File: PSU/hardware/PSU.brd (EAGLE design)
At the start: 143.5 x 58.5 mm, 211 parts, among them J1 SWD, J2 UART, Q1 PMOS-DPAK, Q10 PMOS-SOT23, Q11 NPN, Q12 PMOS-SOT23, Q13 NPN, Q14 NPN, Q15 PMOS-SOT23, Q2 PMOS-SOT23, Q3 NPN, Q4 PMOS-SOT23, Q5 NMOS-SOT23, Q6 PMOS-DPAK, Q7 PMOS-SOT23, Q8 NMOS-SOT23, Q9 PMOS-DPAK, U1 LM2576, U10 4069, U11 LTV-247, U12 74HC08, U13 STM8S003K3T6C, U14 74HC08, U15 4051, U16 358, U17 358, U18 74HC32, U2 MT3608, U3 7805, U4 324, U5 MC34063, U6 MT3608, U7 LM2576, U8 MC34063, U9 TP4056

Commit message: [HW/PSU] Add switch debouncing
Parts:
- added C28, C29: 100n, rcl:C0805
- added R82: 100k, rcl:R0805
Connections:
- net GND: now also C28.2, C29.2, R82.1
- net VBACKUP: now also R82.2
- net ^HDDON: now also C29.1
- net ^PWRON: now also C28.1
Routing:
- net VBACKUP: track 178.1 -> 180.3 mm
- net ^HDDON: track 66.6 -> 68.4 mm
- net ^PWRON: track 48.6 -> 50.0 mm

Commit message: [HW/PSU] Correct resistor values
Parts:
- R1: value 10k -> 47k
- R12: value 2.2k -> 330
- R3: value 3.3k -> 15k
- R64: value 2.2k -> 9.1k
- R68: value 6.8k -> 30k
- R77, R79: value 10k -> 100k
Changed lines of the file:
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@@
 <attribute name="NAME" x="128.27" y="26.67" size="1" layer="26" font="vector" ratio="10" rot="MR0" align="bottom-center"/>
 </element>
-<element name="R1" library="rcl" library_urn="urn:adsk.eagle:library:334" package="R0805" package3d_urn="urn:adsk.eagle:package:23553/2" value="10k" x="109.22" y="22.225" smashed="yes" rot="R90">
+<element name="R1" library="rcl" library_urn="urn:adsk.eagle:library:334" package="R0805" package3d_urn="urn:adsk.eagle:package:23553/2" value="47k" x="109.22" y="22.225" smashed="yes" rot="R90">
 <attribute name="NAME" x="109.22" y="24.384" size="0.8128" layer="25" font="vector" ratio="10" align="bottom-center"/>
 <attribute name="POPULARITY" value="86" x="90.17" y="-3.175" size="0.254" layer="156" font="vector" ratio="10" rot="R90" display="off"/>
 <attribute name="SPICEPREFIX" value="R" x="90.17" y="-3.175" size="0.254" layer="156" font="vector" ratio="10" rot="R90" display="off"/>
 </element>
-<element name="R3" library="rcl" library_urn="urn:adsk.eagle:library:334" package="R0805" package3d_urn="urn:adsk.eagle:package:23553/2" value="3.3k" x="111.76" y="22.86" smashed="yes" rot="R90">
+<element name="R3" library="rcl" library_urn="urn:adsk.eagle:library:334" package="R0805" package3d_urn="urn:adsk.eagle:package:23553/2" value="15k" x="111.76" y="22.86" smashed="yes" rot="R90">
 <attribute name="NAME" x="111.76" y="25.019" size="0.8128" layer="25" font="vector" ratio="10" align="bottom-center"/>
 <attribute name="POPULARITY" value="86" x="97.79" y="-15.24" size="0.254" layer="156" font="vector" ratio="10" rot="R90" display="off"/>
@@
 <attribute name="SPICEPREFIX" value="R" x="63.5" y="14.605" size="0.254" layer="156" font="vector" ratio="10" rot="MR180" display="off"/>
 </element>
-<element name="R64" library="rcl" library_urn="urn:adsk.eagle:library:334" package="R0805" package3d_urn="urn:adsk.eagle:package:23553/2" value="2.2k" x="69.85" y="13.97" smashed="yes" rot="MR270">
+<element name="R64" library="rcl" library_urn="urn:adsk.eagle:library:334" package="R0805" package3d_urn="urn:adsk.eagle:package:23553/2" value="9.1k" x="69.85" y="13.97" smashed="yes" rot="MR270">
 <attribute name="NAME" x="69.85" y="16.129" size="0.8128" layer="26" font="vector" ratio="10" rot="MR0" align="bottom-center"/>
 <attribute name="POPULARITY" value="86" x="69.85" y="13.97" size="0.254" layer="156" font="vector" ratio="10" rot="MR270" display="off"/>
 <attribute name="SPICEPREFIX" value="R" x="69.85" y="13.97" size="0.254" layer="156" font="vector" ratio="10" rot="MR270" display="off"/>
 </element>
-<element name="R68" library="rcl" library_urn="urn:adsk.eagle:library:334" package="R0805" package3d_urn="urn:adsk.eagle:package:23553/2" value="6.8k" x="73.025" y="15.875" smashed="yes" rot="MR180">
+<element name="R68" library="rcl" library_urn="urn:adsk.eagle:library:334" package="R0805" package3d_urn="urn:adsk.eagle:package:23553/2" value="30k" x="73.025" y="15.875" smashed="yes" rot="MR180">
 <attribute name="NAME" x="73.025" y="17.018" size="0.8128" layer="26" font="vector" ratio="10" rot="MR0" align="bottom-center"/>
 <attribute name="POPULARITY" value="86" x="73.025" y="15.875" size="0.254" layer="156" font="vector" ratio="10" rot="MR180" display="off"/>
@@
 <attribute name="POPULARITY" value="15" x="108.585" y="29.845" size="0.254" layer="156" font="vector" ratio="10" display="off"/>
 </element>
-<element name="R12" library="rcl" library_urn="urn:adsk.eagle:library:334" package="R0805" package3d_urn="urn:adsk.eagle:package:23553/2" value="2.2k" x="86.995" y="30.48" smashed="yes" rot="MR270">
+<element name="R12" library="rcl" library_urn="urn:adsk.eagle:library:334" package="R0805" package3d_urn="urn:adsk.eagle:package:23553/2" value="330" x="86.995" y="30.48" smashed="yes" rot="MR270">
 <attribute name="NAME" x="86.995" y="28.321" size="0.8128" layer="26" font="vector" ratio="10" rot="MR180" align="bottom-center"/>
 <attribute name="POPULARITY" value="86" x="86.995" y="30.48" size="0.254" layer="156" font="vector" ratio="10" rot="MR270" display="off"/>
@@
 <attribute name="PROD_ID" value="TRANS-08049" x="38.735" y="41.275" size="0.254" layer="156" font="vector" rot="MR0" display="off"/>
 </element>
-<element name="R77" library="rcl" library_urn="urn:adsk.eagle:library:334" package="R0805" package3d_urn="urn:adsk.eagle:package:23553/2" value="10k" x="37.465" y="47.625" smashed="yes" rot="MR90">
+<element name="R77" library="rcl" library_urn="urn:adsk.eagle:library:334" package="R0805" package3d_urn="urn:adsk.eagle:package:23553/2" value="100k" x="37.465" y="47.625" smashed="yes" rot="MR90">
 <attribute name="NAME" x="37.465" y="49.657" size="0.8128" layer="26" font="vector" ratio="10" rot="MR0" align="bottom-center"/>
 <attribute name="POPULARITY" value="86" x="37.465" y="47.625" size="0.254" layer="156" font="vector" rot="MR90" display="off"/>
@@
 <attribute name="SPICEPREFIX" value="R" x="43.18" y="38.1" size="0.254" layer="156" font="vector" ratio="10" rot="MR180" display="off"/>
 </element>
-<element name="R79" library="rcl" library_urn="urn:adsk.eagle:library:334" package="R0805" package3d_urn="urn:adsk.eagle:package:23553/2" value="10k" x="67.945" y="40.64" smashed="yes" rot="MR270">
+<element name="R79" library="rcl" library_urn="urn:adsk.eagle:library:334" package="R0805" package3d_urn="urn:adsk.eagle:package:23553/2" value="100k" x="67.945" y="40.64" smashed="yes" rot="MR270">
 <attribute name="NAME" x="67.945" y="42.672" size="0.8128" layer="26" font="vector" rot="MR0" align="bottom-center"/>
 <attribute name="POPULARITY" value="86" x="67.945" y="40.64" size="0.254" layer="156" font="vector" ratio="10" rot="MR270" display="off"/>

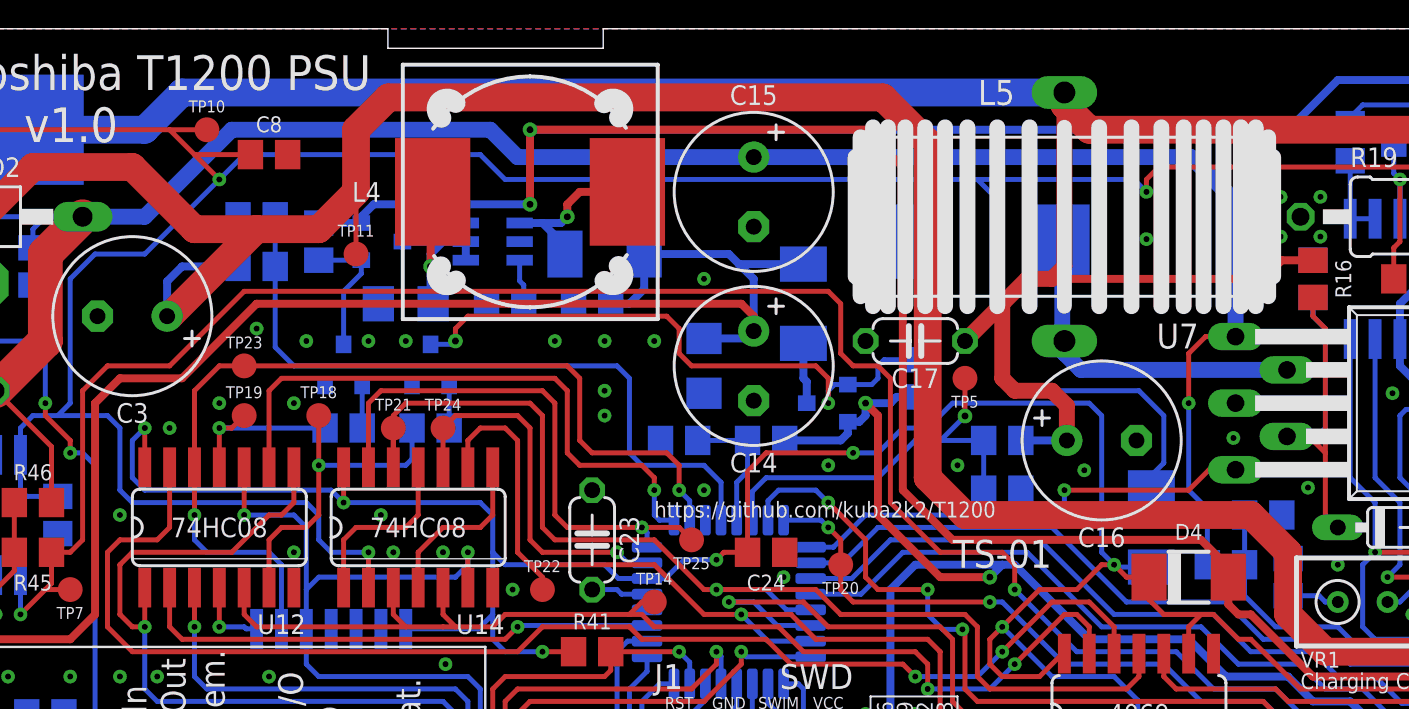
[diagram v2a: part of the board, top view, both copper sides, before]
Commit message: [HW/PSU] Fix Vbat to Vin voltage leak
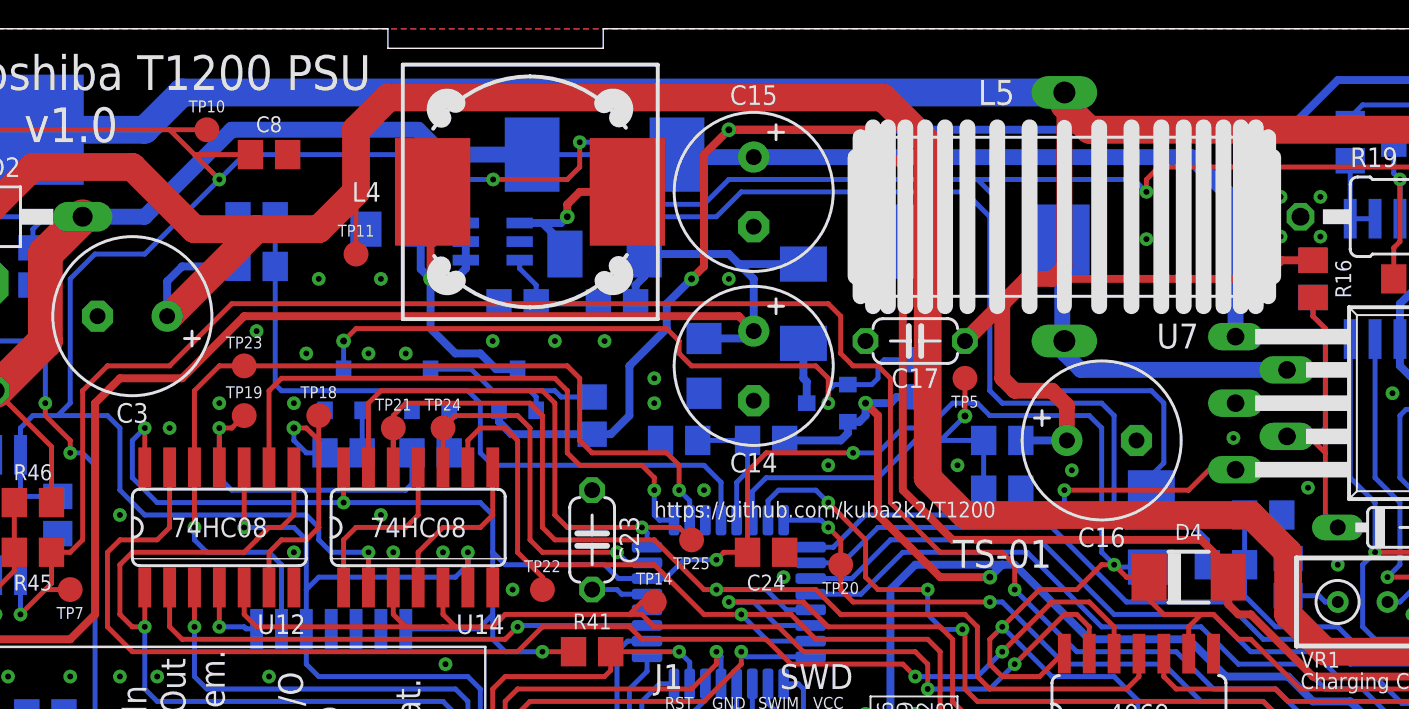
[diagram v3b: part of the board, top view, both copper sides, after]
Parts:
- added D18: SS34, custom:SMC
- moved R77 16.6 mm to (51.4, 38.7), turned to 270 degrees
- moved Q12 10.3 mm to (47.6, 40.0), turned to 0 degrees
- moved R78 4.62 mm to (43.2, 36.8)
- moved R80 4.62 mm to (38.7, 36.8)
- moved Q13 4.62 mm to (43.2, 40.0)
- moved Q14 4.62 mm to (38.7, 40.0)
- moved C12 3.86 mm to (41.3, 48.3)
- moved R15 1.27 mm to (52.7, 44.5)
- moved R18 0.63 mm to (47.6, 44.5)
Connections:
- new net VINCHG: C15.+, D18.C, U7.1
- net VIN: now also D18.A; no longer C15.+, U7.1
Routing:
- net VINCHG: track 0.00 -> 36.4 mm
- net VBACKUP: track 180.3 -> 169.4 mm
- net MEM_BACKUP: track 8.94 -> 17.9 mm
- net VBACKUP_SW: track 11.5 -> 18.5 mm
- net +5VMEM_G: track 30.7 -> 35.3 mm
- net VCCINT: track 226.8 -> 231.3 mm, vias 4 -> 6
- net VIN: track 113.8 -> 110.3 mm, vias 1 -> 0
- net VBACKUP_SW_G: track 6.85 -> 9.97 mm
- net MEM_MAIN: track 17.1 -> 14.6 mm
- net +5V_MEM: track 120.3 -> 118.2 mm
- net MB_FB: track 4.86 -> 5.75 mm
- net AIN_IBUS: track 114.4 -> 113.5 mm
- net GND: vias 105 -> 107
